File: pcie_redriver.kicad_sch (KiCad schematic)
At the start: 75 parts, among them U39 PI3EQX16904GL, U40 PI3EQX16904GL

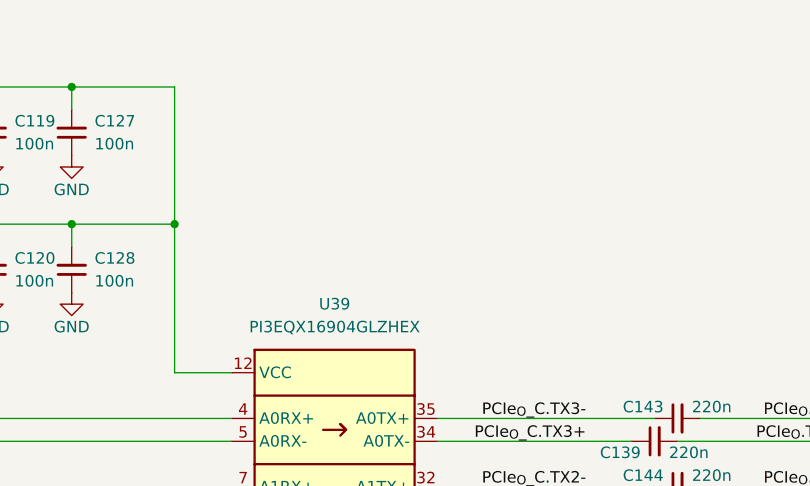
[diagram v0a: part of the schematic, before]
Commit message: [#70030] Unify functional block names
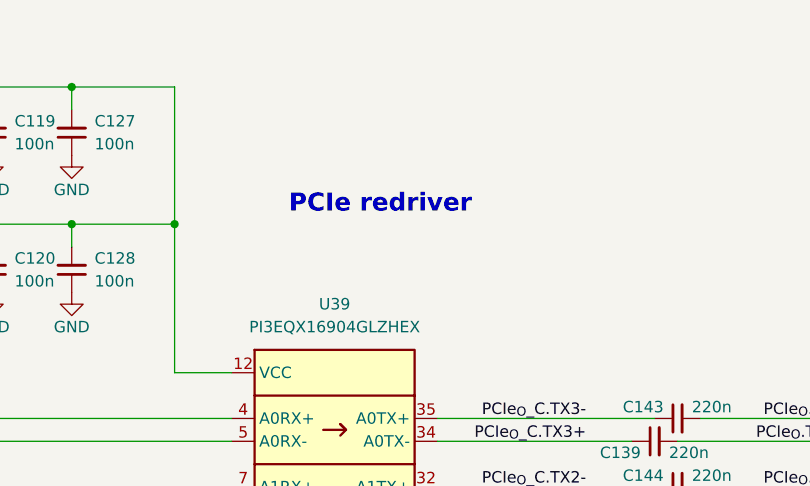
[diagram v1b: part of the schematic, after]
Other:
- note added: "PCIe redriver"
- company: Antmicro Ltd. -> Antmicro Ltd
- title: Com Express 7 baseboard -> COM Express 7 Baseboard
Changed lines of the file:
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@@
 	(paper "A3")
 	(title_block
-		(title "Com Express 7 baseboard")
-		(date "2024-03-28")
+		(title "COM Express 7 Baseboard")
+		(date "2024-12-13")
 		(rev "1.1.0")
-		(company "Antmicro Ltd.")
+		(company "Antmicro Ltd")
+		(comment 1 "www.antmicro.com")
 	)
 	(junction
@@
 			)
 			(justify left bottom)
+		)
+	)
+	(text "PCIe redriver"
+		(exclude_from_sim no)
+		(at 191.77 37.084 0)
+		(effects
+			(font
+				(size 2 2)
+				(thickness 0.8)
+				(bold yes)
+			)
+			(justify left bottom)
